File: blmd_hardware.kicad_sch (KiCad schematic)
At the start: 4 parts, among them IC16 Si8620BB-B-IS, U2 BDJ2FC0WEFJ-E2

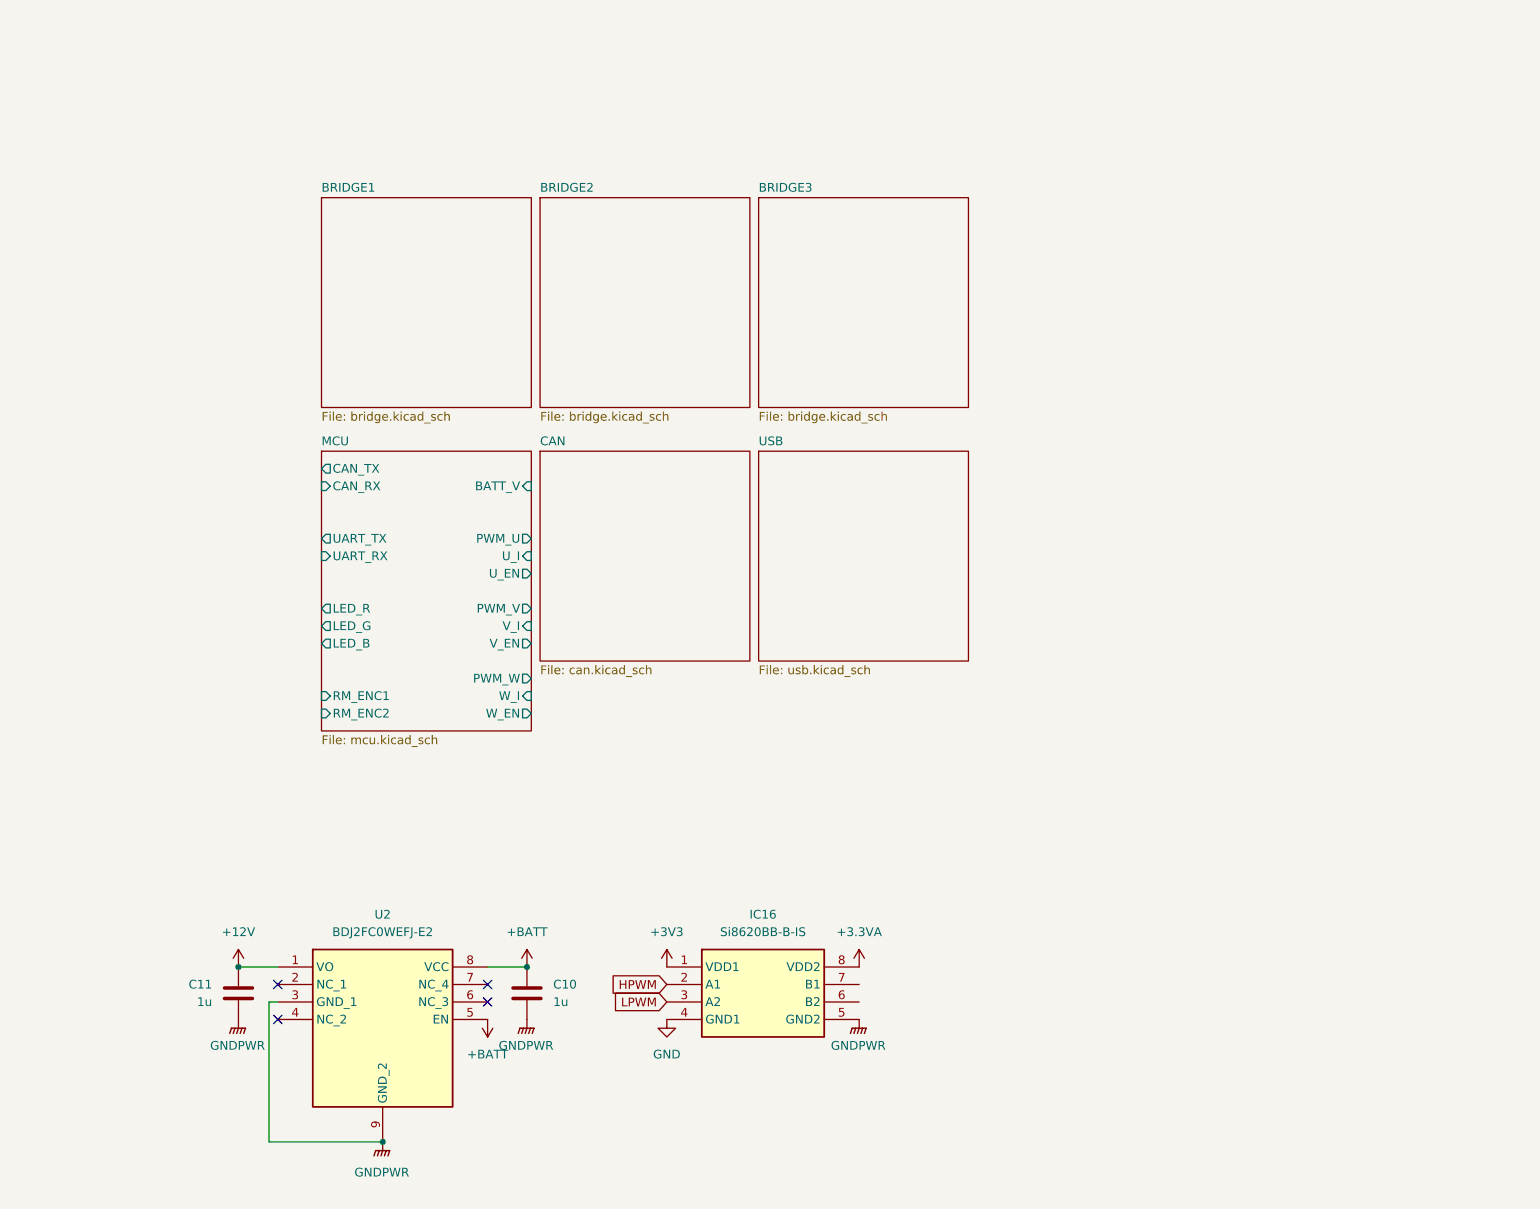
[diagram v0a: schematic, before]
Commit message: 回路図ほぼ完成 MOSFETのゲート抵抗の決め方よくわかんないです助けて
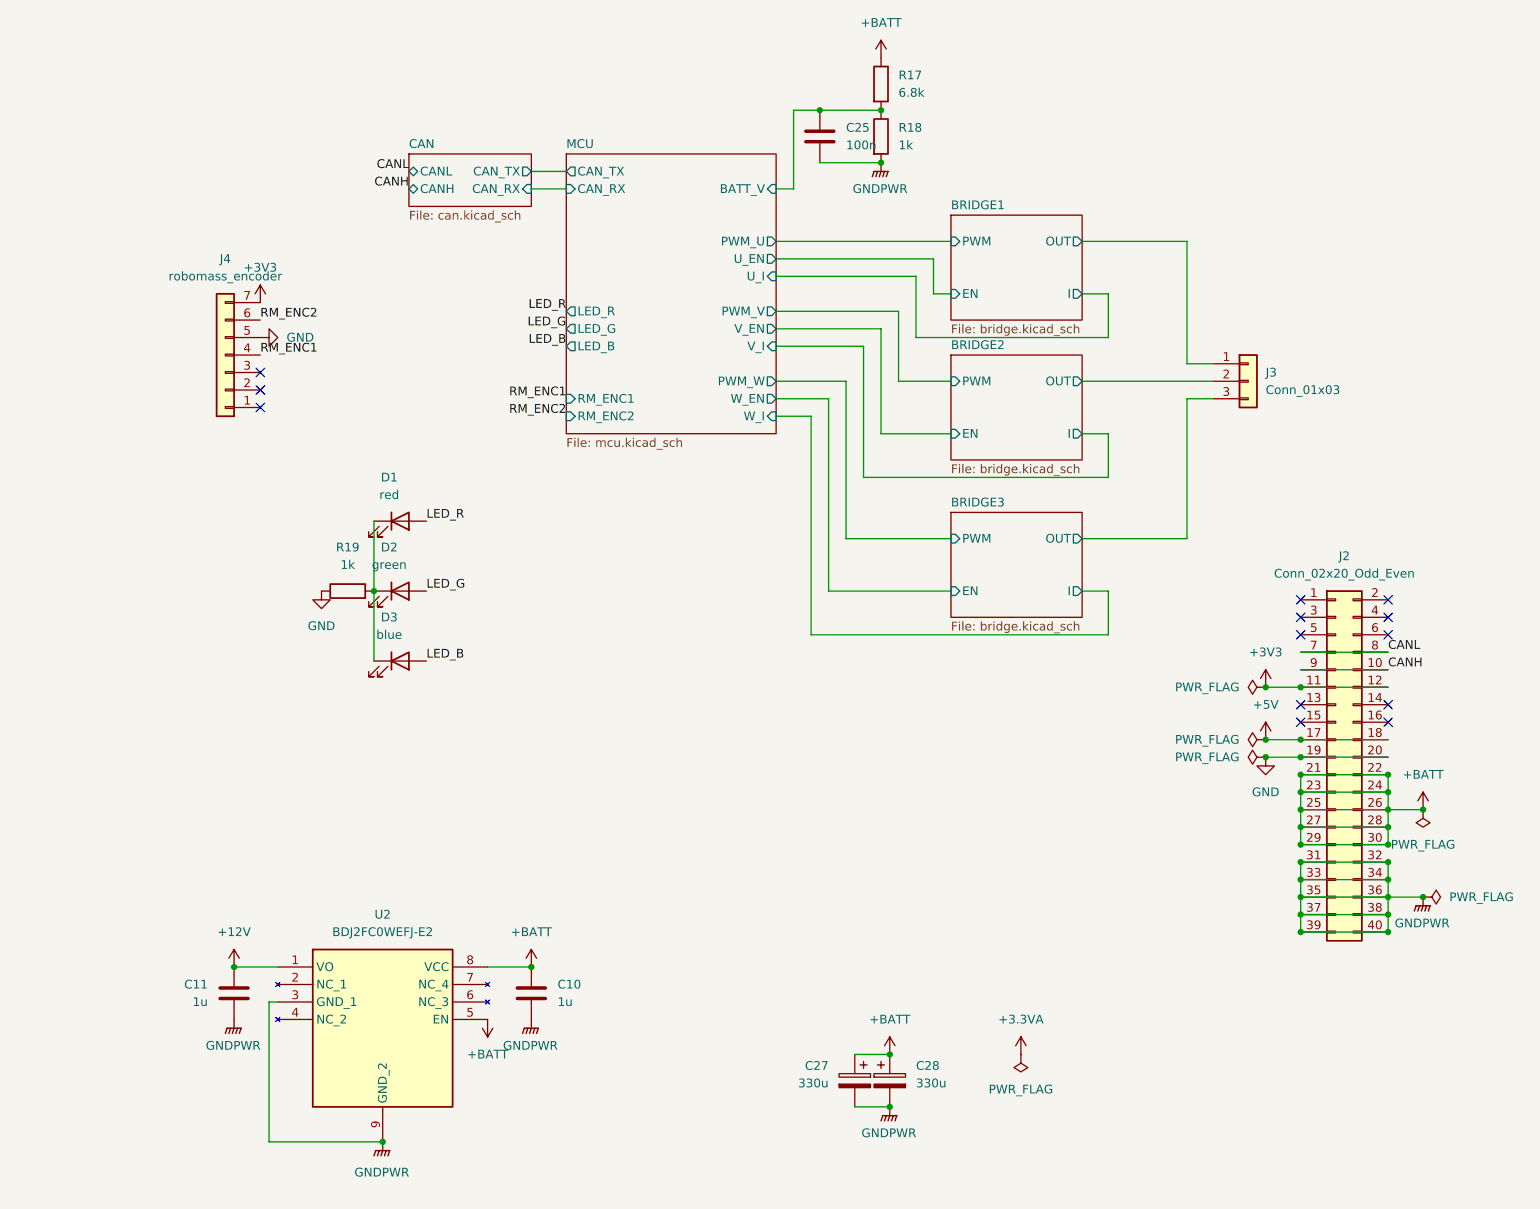
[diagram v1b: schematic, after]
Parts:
- removed IC16: Si8620BB-B-IS, SOIC127P600X175-8N, symbol Si8620BB-B-IS:Si8620BB-B-IS
- added C25: 100n, symbol Device:C
- added C27, C28: 330u, symbol Device:C_Polarized
- added D1: red, symbol Device:LED
- added D2: green, symbol Device:LED
- added D3: blue, symbol Device:LED
- added J2: Conn_02x20_Odd_Even, symbol Connector_Generic:Conn_02x20_Odd_Even
- added J3: Conn_01x03, symbol Connector_Generic:Conn_01x03
- added J4: robomass_encoder, symbol Connector_Generic:Conn_01x07
- added R17: 6.8k, symbol Device:R
- added R18, R19: 1k, symbol Device:R
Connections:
- net +3V3: now also J2.11 (Pin_11), J2.12 (Pin_12), J4.7 (Pin_7)
- net +BATT: now also C27.1, C28.1, J2.21 (Pin_21), J2.22 (Pin_22), J2.23 (Pin_23), J2.24 (Pin_24), J2.25 (Pin_25), J2.26 (Pin_26), J2.27 (Pin_27), J2.28 (Pin_28), J2.29 (Pin_29), J2.30 (Pin_30), R17.1
- net GND: now also J2.19 (Pin_19), J2.20 (Pin_20), J4.5 (Pin_5), R19.1
- net GNDPWR: now also C25.2, C27.2, C28.2, J2.31 (Pin_31), J2.32 (Pin_32), J2.33 (Pin_33), J2.34 (Pin_34), J2.35 (Pin_35), J2.36 (Pin_36), J2.37 (Pin_37), J2.38 (Pin_38), J2.39 (Pin_39), J2.40 (Pin_40), R18.2
- net MCU/BATT_V: now also C25.1, R17.2, R18.1
- new net: D1.1 (K), D2.1 (K), D3.1 (K), R19.2
- new net +5V: J2.17 (Pin_17), J2.18 (Pin_18)
- new net BRIDGE1/OUT: J3.1 (Pin_1)
- new net BRIDGE2/OUT: J3.2 (Pin_2)
- new net BRIDGE3/OUT: J3.3 (Pin_3)
- new net CANH: J2.10 (Pin_10), J2.9 (Pin_9)
- new net CANL: J2.7 (Pin_7), J2.8 (Pin_8)
- new net LED_B: D3.2 (A)
- new net LED_G: D2.2 (A)
- new net LED_R: D1.2 (A)
- new net RM_ENC1: J4.4 (Pin_4)
- new net RM_ENC2: J4.6 (Pin_6)
- no-connect marks 4 -> 13
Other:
- removed sheet USB
- sheet BRIDGE1 ports: added EN, I, OUT, PWM; removed none
- sheet BRIDGE2 ports: added EN, I, OUT, PWM; removed none
- sheet BRIDGE3 ports: added EN, I, OUT, PWM; removed none
- sheet CAN ports: added CANH, CANL, CAN_RX, CAN_TX; removed none
- sheet MCU ports: added none; removed UART_RX, UART_TX
- moved on the sheet: C10, C11

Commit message: 部品配置完了(暫定)
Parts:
- removed C28: 330u, symbol Device:C_Polarized
- removed J4: robomass_encoder, symbol Connector_Generic:Conn_01x07
- added J4: Conn_01x07_MountingPin, Connector_JST:JST_GH_SM07B-GHS-TB_1x07-1MP_P1.25mm_Horizontal, symbol Connector_Generic_MountingPin:Conn_01x07_MountingPin
- added R11, R14: 1k, Resistor_SMD:R_0603_1608Metric_Pad0.98x0.95mm_HandSolder, symbol Device:R
- C10, C11, C25: footprint (none) -> Capacitor_SMD:C_0603_1608Metric_Pad1.08x0.95mm_HandSolder
- C27: footprint (none) -> Capacitor_SMD:CP_Elec_10x12.6
- D1, D2, D3: footprint (none) -> LED_SMD:LED_0603_1608Metric_Pad1.05x0.95mm_HandSolder
- J2: footprint (none) -> Connector_PinHeader_2.54mm:PinHeader_2x20_P2.54mm_Horizontal
- J3: value Conn_01x03 -> BLMD_OUT; footprint (none) -> Connector_AMASS:AMASS_MR30PW-FB_1x03_P3.50mm_Horizontal
- R17, R18, R19: footprint (none) -> Resistor_SMD:R_0603_1608Metric_Pad0.98x0.95mm_HandSolder
- U2: footprint SOIC127P600X100-9N -> samacsys_lib:SOIC127P600X100-9N
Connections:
- net +3.3VA: now also R11.2
- net +3V3: now also J4.7 (Pin_7)
- net GND: now also J4.5 (Pin_5), J4.MP (MountPin)
- net GNDPWR: now also R14.1
- net RM_ENC1: now also J4.4 (Pin_4)
- net RM_ENC2: now also J4.6 (Pin_6)
- new net OP_REF: R11.1, R14.2
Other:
- moved on the sheet: C27
